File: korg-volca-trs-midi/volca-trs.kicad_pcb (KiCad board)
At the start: 2 copper layers, 15 x 15 mm, 2 parts, among them J1 DIN-5_180degree, J2 AudioJack3

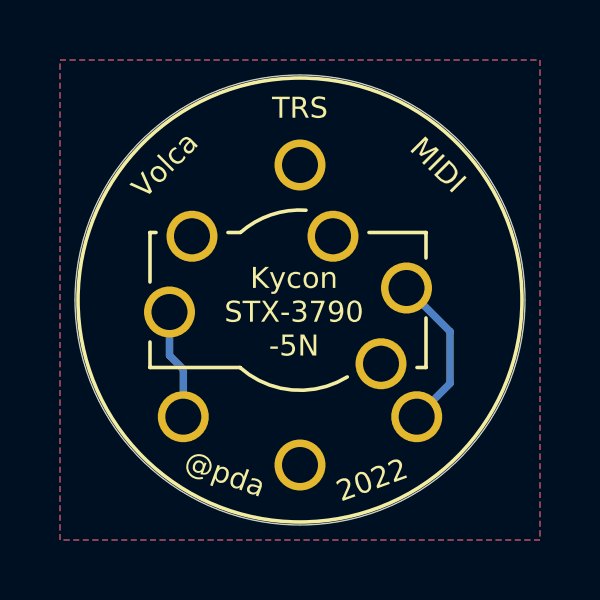
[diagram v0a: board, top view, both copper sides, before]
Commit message: korg-volca-trs-midi: v2! don't connect DIN jack shield to GND
MIDI cables shield the signal with ground, but that doesn't mean the
sleeve of the DIN jack is also connected to GND. The previous revision
connected them, and I suspect that's the culprit of terrible noise
interference when connected.

(I confirmed the original Volca MIDI DIN jack sleeve/shield is not
connected to MIDI GND, nor to the battery negative terminal, which may
or may not mean anything).
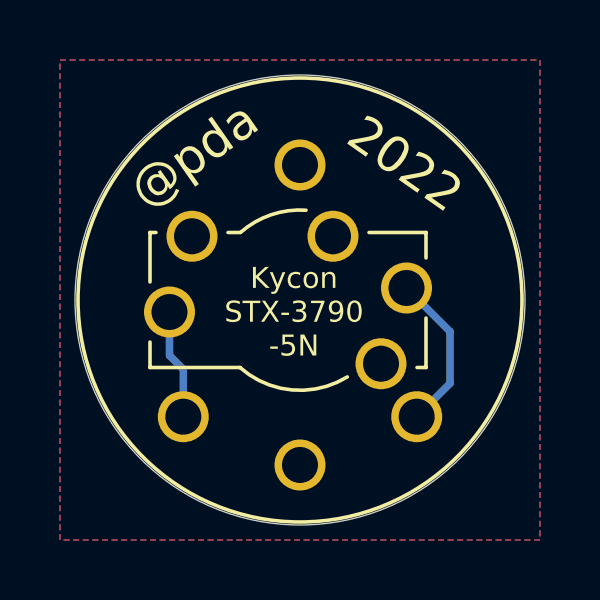
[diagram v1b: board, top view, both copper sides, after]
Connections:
- J1 pad S: /SLEEVE -> (no net)
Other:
- board text added: "Volca TRS MIDI"
- board text removed: "MIDI"
- board text removed: "TRS"
- board text removed: "Volca"
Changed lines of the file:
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@@
     (pad "5" thru_hole circle (at -3.89 3.89) (size 1.7 1.7) (drill 1.2) (layers *.Cu *.Mask)
       (net 3 "/TIP") (pintype "passive"))
-    (pad "S" thru_hole circle (at 0 -4.5) (size 1.7 1.7) (drill 1.2) (layers *.Cu *.Mask)
-      (net 1 "/SLEEVE"))
+    (pad "S" thru_hole circle (at 0 -4.5) (size 1.7 1.7) (drill 1.2) (layers *.Cu *.Mask))
   )
   (footprint "Library:3.5mm TRS STX-3790-5N" (layer "F.Cu")
@@
       (net 1 "/SLEEVE"))
   )
+  (gr_line (start 40.792673 44.742705) (end 41.153744 44.379036) (layer "B.SilkS") (width 0.15))
   (gr_line (start 36.1 42.3) (end 35.64109 41.84139) (layer "B.SilkS") (width 0.15))
   (gr_line (start 44.989644 41.037054) (end 44.299338 40.346682) (layer "B.SilkS") (width 0.15))
-  (gr_line (start 40 44.4) (end 40 39) (layer "B.SilkS") (width 0.15))
+  (gr_line (start 41.153744 44.379036) (end 41.153744 38.979036) (layer "B.SilkS") (width 0.15))
   (gr_line (start 36.1 42.8) (end 36.1 42.3) (layer "B.SilkS") (width 0.15))
-  (gr_line (start 40 39) (end 40.36942 38.628746) (layer "B.SilkS") (width 0.15))
   (gr_line (start 35.64109 41.84139) (end 35.64109 41.456633) (layer "B.SilkS") (width 0.15))
   (gr_line (start 44.628573 43.141562) (end 44.989644 42.777893) (layer "B.SilkS") (width 0.15))
@@
     (effects (font (size 1 1) (thickness 0.1)) (justify mirror))
   )
-  (gr_text "2" (at 38.6 46.2) (layer "B.SilkS")
+  (gr_text "2" (at 41.481804 45.536896) (layer "B.SilkS")
     (effects (font (size 1 1) (thickness 0.1)) (justify mirror))
   )
-  (gr_text "S" (at 39.7 37.9) (layer "B.SilkS")
+  (gr_text "S" (at 42.523879 37.914315) (layer "B.SilkS")
     (effects (font (size 1 1) (thickness 0.1)) (justify mirror))
   )
@@
     (effects (font (size 1 1) (thickness 0.1)) (justify mirror))
   )
-  (gr_text "S" (at 38.6 35.6) (layer "B.SilkS")
-    (effects (font (size 1 1) (thickness 0.1)) (justify mirror))
+  (gr_text "Volca\nTRS MIDI" (at 38.432772 40.94405 90) (layer "B.SilkS")
+    (effects (font (size 1 1) (thickness 0.2)) (justify mirror))
   )
-  (gr_text "TRS" (at 40 33.6) (layer "F.SilkS")
-    (effects (font (size 0.7 0.7) (thickness 0.1)))
+  (gr_text "2022" (at 43.50806 35.463511 -35) (layer "F.SilkS")
+    (effects (font (size 1.2 1.2) (thickness 0.2)))
   )
   (gr_text "Kycon\nSTX-3790\n-5N" (at 39.8 40.4) (layer "F.SilkS")
     (effects (font (size 0.7 0.7) (thickness 0.1)))
   )
-  (gr_text "@pda" (at 37.5 45.8 -20) (layer "F.SilkS")
-    (effects (font (size 0.7 0.7) (thickness 0.1)))
-  )
-  (gr_text "Volca" (at 35.5 35.5 45) (layer "F.SilkS")
-    (effects (font (size 0.7 0.7) (thickness 0.1)))
-  )
-  (gr_text "MIDI" (at 44.6 35.5 -45) (layer "F.SilkS")
-    (effects (font (size 0.7 0.7) (thickness 0.1)))
-  )
-  (gr_text "2022" (at 42.4 46 20) (layer "F.SilkS")
-    (effects (font (size 0.7 0.7) (thickness 0.1)))
+  (gr_text "@pda" (at 36.46441 35.154748 35) (layer "F.SilkS")
+    (effects (font (size 1.2 1.2) (thickness 0.2)))
   )
   (segment (start 43.89 43.89) (end 45 42.78) (width 0.25) (layer "B.Cu") (net 2))
